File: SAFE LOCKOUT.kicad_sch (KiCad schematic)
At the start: 41 parts, among them J1 Conn_01x12_Pin, J2 Conn_01x02_Pin, J3 Conn_01x02_Pin, J4 Conn_01x02_Pin, J5 Conn_01x02_Pin, J6 Conn_01x02_Pin, J7 Conn_01x02_Pin, J8 Conn_01x02_Pin, J9 Conn_01x02_Pin, K1 PR30-24V-450-1A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

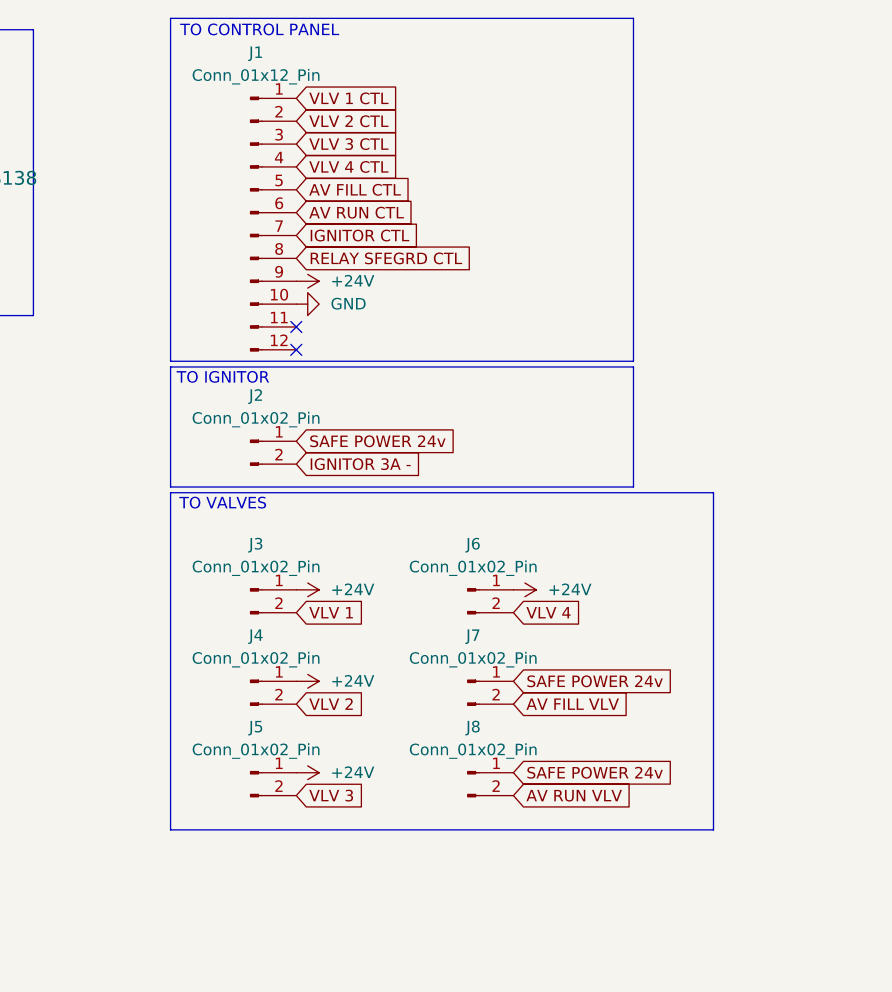
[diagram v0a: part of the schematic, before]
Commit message: changed power source and footprints
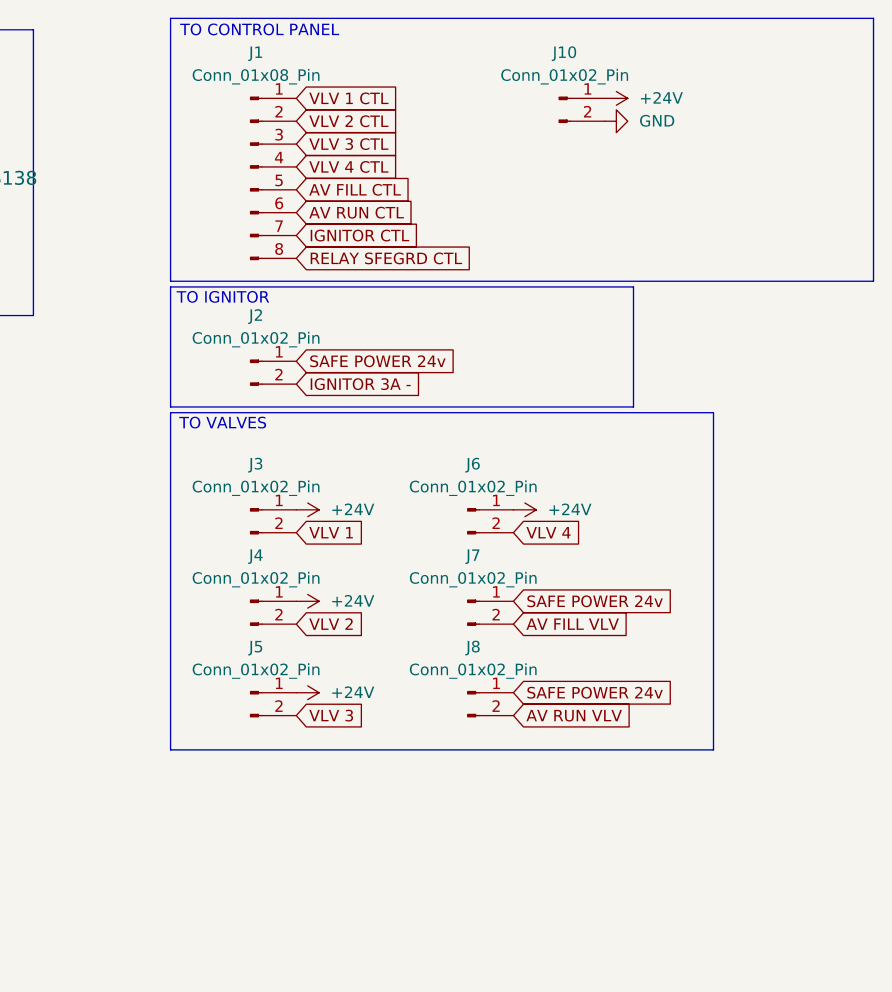
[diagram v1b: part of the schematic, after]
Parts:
- removed J1: Conn_01x12_Pin, Connector_Phoenix_MSTB:PhoenixContact_MSTBA_2,5_12-G-5,08_1x12_P5.08mm_Horizontal, symbol Connector:Conn_01x12_Pin
- added J1: Conn_01x08_Pin, Connector_Molex:Molex_Micro-Fit_3.0_43045-1600_2x08_P3.00mm_Horizontal, symbol Connector:Conn_01x08_Pin
- added J10: Conn_01x02_Pin, Connector_Molex:Molex_Micro-Fit_3.0_43650-0200_1x02_P3.00mm_Horizontal, symbol Connector:Conn_01x02_Pin
- J2, J3, J4, J5, J6, J7, J8, J9: footprint Connector_Phoenix_MSTB:PhoenixContact_MSTBA_2,5_2-G-5,08_1x02_P5.08mm_Horizontal -> Connector_JST:JST_XH_B2B-XH-AM_1x02_P2.50mm_Vertical
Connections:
- net +24V: now also J10.1 (Pin_1)
- net AV  RUN CTL: now also J1.6 (Pin_6)
- net AV FILL CTL: now also J1.5 (Pin_5)
- net GND: now also J10.2 (Pin_2)
- net IGNITOR CTL: now also J1.7 (Pin_7)
- net RELAY SFEGRD CTL: now also J1.8 (Pin_8)
- net VLV 1 CTL: now also J1.1 (Pin_1)
- net VLV 2 CTL: now also J1.2 (Pin_2)
- net VLV 3 CTL: now also J1.3 (Pin_3)
- net VLV 4 CTL: now also J1.4 (Pin_4)
- no-connect marks 2 -> 0
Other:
- moved on the sheet: J2, J3, J4, J5, J6, J7, J8

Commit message: changed screw terminal
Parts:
- J9: footprint Connector_JST:JST_XH_B2B-XH-AM_1x02_P2.50mm_Vertical -> Connector_Phoenix_MSTB:PhoenixContact_MSTBVA_2,5_2-G_1x02_P5.00mm_Vertical
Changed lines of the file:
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@@
 			)
 		)
-		(property "Footprint" "Connector_JST:JST_XH_B2B-XH-AM_1x02_P2.50mm_Vertical"
+		(property "Footprint" "Connector_Phoenix_MSTB:PhoenixContact_MSTBVA_2,5_2-G_1x02_P5.00mm_Vertical"
 			(at 31.75 165.1 0)
 			(effects

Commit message: logan did pcb, some suff still needs to be fixed
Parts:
- removed J1: Conn_01x08_Pin, Connector_Molex:Molex_Micro-Fit_3.0_43045-1600_2x08_P3.00mm_Horizontal, symbol Connector:Conn_01x08_Pin
- added J1: Conn_01x12_Pin, 430451200:MOLEX_430451200, symbol Connector:Conn_01x12_Pin
- D1, D2, D3, D4, D5, D6, D7: footprint digikey-footprints:DO-214AC -> Solenoid Safeguard:DO-214AC
- J2: footprint Connector_JST:JST_XH_B2B-XH-AM_1x02_P2.50mm_Vertical -> Connector_Molex:Molex_Micro-Fit_3.0_43650-0200_1x02_P3.00mm_Horizontal
- J9: footprint Connector_Phoenix_MSTB:PhoenixContact_MSTBVA_2,5_2-G_1x02_P5.00mm_Vertical -> Kinky:PhoenixContact_MSTBVA_2,5_2-G_1x02_P5.00mm_Vertical
- K1: footprint PR30_24V_450_1A:RELAY_PR30-24V-450-1A -> Solenoid Safeguard:RELAY_PR30-24V-450-1A
- Q1, Q2, Q3, Q4, Q5, Q6, Q7, Q8: footprint digikey-footprints:SOT-23-3 -> Package_TO_SOT_SMD:SOT-23-3
- R1, R11, R13, R15, R3, R5, R7, R9: footprint PCM_JLCPCB:R_0805 -> Solenoid Safeguard:R_0805
- R10, R12, R14, R16, R2, R4, R6, R8: footprint Resistor_SMD:R_0402_1005Metric -> Solenoid Safeguard:R_0805
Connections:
- net AV  RUN CTL: now also J1.8 (Pin_8)
- net AV FILL CTL: now also J1.7 (Pin_7)
- net GND: now also J1.1 (Pin_1)
- net IGNITOR CTL: now also J1.2 (Pin_2)
- net RELAY SFEGRD CTL: now also J1.3 (Pin_3)
- net VLV 1 CTL: now also J1.12 (Pin_12)
- net VLV 2 CTL: now also J1.11 (Pin_11)
- net VLV 3 CTL: now also J1.10 (Pin_10)
- net VLV 4 CTL: now also J1.9 (Pin_9)
- no-connect marks 0 -> 3
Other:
- moved on the sheet: J2, J3, J4, J5, J6, J7, J8
